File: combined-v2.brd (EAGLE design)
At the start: 0 parts

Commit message: v2 of board finished
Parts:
- added 100POT1_COMP1, 100POT1_COMP2, 100POT1_COMP3, 100POT1_COMP5: MCP42100-I/P, MCP42100-I_P:DIP254P762X432-14
- added 10KPOT1_PAN1, 10KPOT1_PAN2, 10KPOT1_PAN3, 10KPOT1_PAN4, 10POT1_COMP1, 10POT1_COMP2, 10POT1_COMP3, 10POT1_COMP5, 10POT2_COMP1, 10POT2_COMP2, 10POT2_COMP3, 10POT2_COMP5: MCP4131-503E/SN, MCP4131-503E_SN:SOIC127P599X175-8N
- added 200POT1_COMP1, 200POT1_COMP2, 200POT1_COMP3, 200POT1_COMP5, 200POT2_COMP1, 200POT2_COMP2, 200POT2_COMP3, 200POT2_COMP5: MAX5419LETA+, MAX5419LETA_:SON65P300X300X80-9N
- added 3V3_D1, 9VDD1, BCK_ADC1, CE_EQ1, CE_EQ2, CLK_ADC1, CS3, CS4, CS5, CS6, DOUT_ADC1, GND4, GND6, LRCK_ADC1, MUX2, MUX3, PAD1, PAD10, PAD11, PAD12, PAD13, PAD14, PAD15, PAD16, PAD2, PAD3, PAD4, PAD5, PAD6, PAD7, PAD8, PAD9, SCK1, SCL1, SCL2, SDA1, SDA2, SDI/O1: (no value), wirepad:SMD1,27-2,54
- added C10, C105, C106, C109, C11, C110, C111, C112, C115, C116, C14, C15, C16, C17, C20, C21: 0.01uF, rcl:C0402
- added C103, C104, C117, C118, C22, C23, C7, C9: 0.047uF, rcl:C0402
- added C107, C108, C113, C114, C12, C13, C18, C19: 0.068uF, rcl:C0402
- added C119, C120, C121, C122, C123, C124, C125, C126, C127, C129, C130, C131, C132, C134, C2, C24, C25, C26, C27, C28, C29, C30, C31, C32, C34, C35, C36, C37, C39, C5, C6, C69, C71, C77, C78, C79, C8, C80, C81, C82, C83, C84: 10uF, rcl:C0402
- added C128, C133, C33, C38, C68, C70, C73: 0.1uF, rcl:C0402
- added C3, C4: 0.1u, rcl:C0402
- added C42, C45, C48, C54: 680p, rcl:C0402
- added C43, C46, C49, C55: 10u, rcl:C0402
- added C44, C47, C50, C56: 1.5u, rcl:C0402
- added C72, C74: 1uF, rcl:C0402
- added C75, C76: 15pF, rcl:C0402
- added D16, D17, D18, D19, D20, D21, D22, D23, D24, D25, D26, D27, D28, D29, D30, D31, D32, D33, D34, D35, D36, D37, D38, D39, D40, D41, D42, D43, D44, D45, D46, D47, D48, D60, D61, D62, D63, D64, D65, D66, D67, D68, D69, D70: 1N4148W-TP, 1N4148W-TP:SOD123
- added D2, D3, D4, D5: 1N4148W-TPSOD123-L, 1N4148W-TP:SOD123-L
- added GND1, GND2, GND3, GND5, GNDL1, GNDR1, IN_COMP1, IN_COMP2, IN_COMP3, IN_COMP5, OUTL_MIX1, OUTR_MIX1: (no value), wirepad:SMD2,54-5,08
- added IC2: PCM1865DBT, PCM1865DBT:TSSOP-30
- added OPAMP1_COMP1, OPAMP1_COMP2, OPAMP1_COMP3, OPAMP1_COMP5, OPAMP1_MIX1, OPAMP1_PAN1, OPAMP1_PAN2, OPAMP1_PAN3, OPAMP1_PAN4, OPAMP2_COMP1, OPAMP2_COMP2, OPAMP2_COMP3, OPAMP2_COMP5, OPAMP3_COMP1, OPAMP3_COMP2, OPAMP3_COMP3, OPAMP3_COMP5, OPAMP4_COMP1, OPAMP4_COMP2, OPAMP4_COMP3, OPAMP4_COMP5, U2: LM4562MAX/NOPB, LM4562MAX_NOPB:SOIC127P599X175-8N
- added R10, R11, R13, R16, R17, R18, R20, R31, R33, R35, R36, R37, R38, R39, R40, R43, R46, R48, R50, R51, R52, R53, R54, R55, R58, R69, R7, R70, R71, R73, R83, R84, R85, R87: 5k, rcl:R0402
- added R100, R102, R103, R104, R107, R108, R109, R111, R112, R113, R117, R118, R120, R121, R122, R125, R126, R127, R129, R130, R149, R153, R154, R156, R157, R158, R161, R162, R163, R165, R166, R63, R67, R75, R77, R78, R79, R89, R90, R91, R93, R94, R95, R99: 100k, rcl:R0402
- added R101, R105, R110, R119, R12, R123, R128, R14, R155, R159, R164, R19, R21, R32, R34, R41, R42, R47, R49, R56, R57, R72, R74, R76, R80, R86, R88, R92: 10k, rcl:R0402
- added R106, R124, R160, R81: 20k, rcl:R0402
- added R114, R116, R150, R152, R64, R66, R96, R98: 470k, rcl:R0402
- added R115, R151, R45, R5, R60, R65, R8, R9, R97: 1k, rcl:R0402
- added R15, R6, R68, R82: 1M, rcl:R0402
- added R22: 1.7k, rcl:R0402
- added R44, R59: 50k, rcl:R0402
- added U$1, U$3: LC75281E, LC75281E:QFP80P1720X1720X270-64N
- added U11, U3, U4, U5: TMUX1204DGSR, TMUX1204DGSR:SOP50P490X110-10N
- added Y2: CM7V-T1A-32.768KHZ-12.5PF-100PPM-TB-QC, CM7V-T1A-32.768KHZ-12.5PF-100PPM-TB-QC:XTAL_CM7V-T1A-32.768KHZ-12.5PF-100PPM-TB-QC
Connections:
- new net +3V3: 3V3_D1.1, U11.5, U11.6, U3.5, U3.6, U4.5, U4.6, U5.5, U5.6
- new net 3V3A: C70.1, C71.1, IC2.8, U2.1, U2.2
- new net 3V3D: C68.1, C69.1, IC2.13, IC2.14
- new net BCK_ADC: BCK_ADC1.1, IC2.17
- new net CLK_ADC: CLK_ADC1.1, IC2.15
- new net CS: CS6.1, U11.8
- new net CS0: CS3.1, U3.8
- new net CS0_COMP1: 100POT1_COMP1.1, U3.2
- new net CS0_COMP2: 100POT1_COMP3.1, U3.9
- new net CS0_COMP3: 100POT1_COMP2.1, U3.4
- new net CS0_COMP4: 100POT1_COMP5.1, U3.7
- new net CS1: CS4.1, U5.8
- new net CS1_COMP1: 10POT1_COMP1.1, U5.2
- new net CS1_COMP2: 10POT1_COMP3.1, U5.9
- new net CS1_COMP3: 10POT1_COMP2.1, U5.4
- new net CS1_COMP4: 10POT1_COMP5.1, U5.7
- new net CS2: CS5.1, U4.8
- new net CS2_COMP1: 10POT2_COMP1.1, U4.2
- new net CS2_COMP2: 10POT2_COMP3.1, U4.9
- new net CS2_COMP3: 10POT2_COMP2.1, U4.4
- new net CS2_COMP4: 10POT2_COMP5.1, U4.7
- new net CS_PAN1: 10KPOT1_PAN1.1, U11.2
- new net CS_PAN2: 10KPOT1_PAN3.1, U11.9
- new net CS_PAN3: 10KPOT1_PAN2.1, U11.4
- new net CS_PAN4: 10KPOT1_PAN4.1, U11.7
- new net DOUT_ADC: DOUT_ADC1.1, IC2.18
- new net EQ1_CE1: CE_EQ1.1, U$1.27
- new net EQ2_CE3: CE_EQ2.1, U$3.27
- new net GND: 100POT1_COMP1.4, 100POT1_COMP2.4, 100POT1_COMP3.4, 100POT1_COMP5.4, 10KPOT1_PAN1.4, 10KPOT1_PAN2.4, 10KPOT1_PAN3.4, 10KPOT1_PAN4.4, 10POT1_COMP1.4, 10POT1_COMP2.4, 10POT1_COMP3.4, 10POT1_COMP5.4, 10POT2_COMP1.4, 10POT2_COMP2.4, 10POT2_COMP3.4, 10POT2_COMP5.4, 200POT1_COMP1.5, 200POT1_COMP1.9, 200POT1_COMP2.5, 200POT1_COMP2.9, 200POT1_COMP3.5, 200POT1_COMP3.9, 200POT1_COMP5.5, 200POT1_COMP5.9, 200POT2_COMP1.4, 200POT2_COMP1.5, 200POT2_COMP1.9, 200POT2_COMP2.4, 200POT2_COMP2.5, 200POT2_COMP2.9, 200POT2_COMP3.4, 200POT2_COMP3.5, 200POT2_COMP3.9, 200POT2_COMP5.4, 200POT2_COMP5.5, 200POT2_COMP5.9, C123.2, C134.2, C28.2, C39.2, C68.2, C69.2, C70.2, C71.2, C72.2, C73.2, C74.2, C75.2, C76.2, GND1.1, GND2.1, GND3.1, GND4.1, GND5.1, GND6.1, GNDL1.1, GNDR1.1, IC2.12, IC2.25, IC2.7, OPAMP1_COMP1.4, OPAMP1_COMP2.4, OPAMP1_COMP3.4, OPAMP1_COMP5.4, OPAMP1_MIX1.4, OPAMP1_PAN1.4, OPAMP1_PAN2.4, OPAMP1_PAN3.4, OPAMP1_PAN4.4, OPAMP2_COMP1.4, OPAMP2_COMP2.4, OPAMP2_COMP3.4, OPAMP2_COMP5.4, OPAMP3_COMP1.4, OPAMP3_COMP2.4, OPAMP3_COMP3.4, OPAMP3_COMP5.4, OPAMP4_COMP1.4, OPAMP4_COMP2.4, OPAMP4_COMP3.4, OPAMP4_COMP5.4, R5.1, R9.1, U$1.21, U$1.28, U$3.21, U$3.28, U11.3, U2.4, U3.3, U4.3, U5.3
- new net H1_COMP1: 200POT1_COMP1.8, 200POT2_COMP1.8, C44.1, OPAMP1_COMP1.6, R66.1
- new net H1_COMP2: 200POT1_COMP3.8, 200POT2_COMP3.8, C50.1, OPAMP1_COMP3.6, R116.1
- new net H1_COMP3: 200POT1_COMP2.8, 200POT2_COMP2.8, C47.1, OPAMP1_COMP2.6, R98.1
- new net H1_COMP4: 200POT1_COMP5.8, 200POT2_COMP5.8, C56.1, OPAMP1_COMP5.6, R152.1
- new net IN_COMP1: C43.2, IN_COMP1.1
- new net IN_COMP2: C49.2, IN_COMP3.1
- new net IN_COMP3: C46.2, IN_COMP2.1
- new net IN_COMP4: C55.2, IN_COMP5.1
- new net L1_COMP1: 200POT1_COMP1.6, 200POT1_COMP1.7, D19.C
- new net L1_COMP2: 200POT1_COMP3.6, 200POT1_COMP3.7, D41.C
- new net L1_COMP3: 200POT1_COMP2.6, 200POT1_COMP2.7, D30.C
- new net L1_COMP4: 200POT1_COMP5.6, 200POT1_COMP5.7, D63.C
- new net L2_COMP1: 200POT2_COMP1.6, 200POT2_COMP1.7, R94.2
- new net L2_COMP2: 200POT2_COMP3.6, 200POT2_COMP3.7, R130.2
- new net L2_COMP3: 200POT2_COMP2.6, 200POT2_COMP2.7, R112.2
- new net L2_COMP4: 200POT2_COMP5.6, 200POT2_COMP5.7, R166.2
- new net LRCK_ADC: IC2.16, LRCK_ADC1.1
- new net MUX0: MUX2.1, U11.1, U3.1, U4.1, U5.1
- new net MUX1: MUX3.1, U11.10, U3.10, U4.10, U5.10
- new net N$10: R32.2, R34.2, R41.2, R42.2, R43.1
- new net N$100: D64.A, D65.C
- new net N$101: C55.1, R163.2
- new net N$102: D68.A, D69.C
- new net N$103: D67.A, D68.C
- new net N$11: R31.2, R38.1, R42.1
- new net N$114: C72.1, IC2.6
- new net N$115: C73.1, C74.1, IC2.11
- new net N$116: C75.1, IC2.9, Y2.2
- new net N$117: C76.1, IC2.10, Y2.1
- new net N$118: C84.2, IC2.1
- new net N$119: C77.2, IC2.2
- new net N$12: R33.2, R37.1, R41.1
- new net N$120: C103.1, U$3.1
- new net N$121: C105.1, U$3.6
- new net N$122: C106.1, U$3.7
- new net N$123: C81.2, IC2.3
- new net N$124: C107.1, U$3.11
- new net N$125: C78.2, IC2.4
- new net N$126: C79.2, IC2.29
- new net N$127: C83.2, IC2.28
- new net N$128: C80.2, IC2.27
- new net N$13: C13.1, U$1.12
- new net N$131: C108.1, U$3.12
- new net N$132: C109.1, U$3.16
- new net N$135: C110.1, U$3.17
- new net N$136: C111.1, U$3.32
- new net N$137: C112.1, U$3.33
- new net N$138: C113.1, U$3.37
- new net N$139: C114.1, U$3.38
- new net N$14: C14.1, U$1.16
- new net N$140: C115.1, U$3.42
- new net N$141: C116.1, U$3.43
- new net N$142: C117.1, U$3.47
- new net N$143: C118.1, U$3.48
- new net N$144: C103.2, U$3.64
- new net N$145: C104.2, C119.2, U$3.3
- new net N$146: C119.1, U$3.4
- new net N$147: C120.1, U$3.9
- new net N$148: C121.1, U$3.14
- new net N$149: C122.1, U$3.19
- new net N$15: C15.1, U$1.17
- new net N$150: C123.1, C134.1, U$3.23
- new net N$151: C124.1, U$3.30
- new net N$152: C125.1, U$3.35
- new net N$153: C126.1, U$3.40
- new net N$154: C127.1, U$3.45
- new net N$155: C128.1, U$3.50
- new net N$156: C129.1, U$3.52
- new net N$157: C130.1, U$3.55
- new net N$158: C131.1, U$3.59
- new net N$159: C132.1, U$3.62
- new net N$16: C16.1, U$1.32
- new net N$160: C133.1, U$3.63
- new net N$161: C105.2, U$3.5
- new net N$162: C106.2, C120.2, U$3.8
- new net N$163: C107.2, U$3.10
- new net N$164: C108.2, C121.2, U$3.13
- new net N$165: C109.2, U$3.15
- new net N$166: C110.2, C122.2, U$3.18
- new net N$167: C111.2, C124.2, U$3.31
- new net N$168: C112.2, U$3.34
- new net N$169: C113.2, C125.2, U$3.36
- new net N$17: C17.1, U$1.33
- new net N$170: C114.2, U$3.39
- new net N$171: C115.2, C126.2, U$3.41
- new net N$172: C116.2, U$3.44
- new net N$173: C117.2, C127.2, U$3.46
- new net N$174: C118.2, U$3.49
- new net N$175: C129.2, U$3.51
- new net N$176: C130.2, U$3.54
- new net N$177: C131.2, U$3.58
- new net N$178: C132.2, U$3.61
- new net N$179: C104.1, U$3.2
- new net N$18: R34.1, R36.1, R40.2
- new net N$183: C82.2, IC2.30
- new net N$19: C4.1, R60.2
- new net N$2: C2.2, R10.2, R6.2, R7.2
- new net N$20: R47.1, R50.2, R54.2
- new net N$21: R47.2, R49.2, R56.2, R57.2, R58.1
- new net N$211: C42.1, D17.A, D18.C, D25.A, R65.1, R89.2
- new net N$212: C48.1, D39.A, D40.C, D47.A, R115.1, R125.2
- new net N$213: C45.1, D28.A, D29.C, D36.A, R107.2, R97.1
- new net N$214: C54.1, D61.A, D62.C, D69.A, R151.1, R161.2
- new net N$22: R46.2, R53.1, R57.1
- new net N$23: R48.2, R52.1, R56.1
- new net N$24: R49.1, R51.1, R55.2
- new net N$25: C18.1, U$1.37
- new net N$26: C6.2, R68.2, R69.2, R70.2
- new net N$27: C19.1, U$1.38
- new net N$28: C8.2, R82.2, R83.2, R84.2
- new net N$29: C20.1, U$1.42
- new net N$3: C5.2, R15.2, R16.2, R17.2
- new net N$30: C21.1, U$1.43
- new net N$31: C22.1, U$1.47
- new net N$32: C23.1, U$1.48
- new net N$33: C7.2, U$1.64
- new net N$34: C24.2, C9.2, U$1.3
- new net N$35: C24.1, U$1.4
- new net N$36: C25.1, U$1.9
- new net N$37: C26.1, U$1.14
- new net N$38: C27.1, U$1.19
- new net N$39: C28.1, C39.1, U$1.23
- new net N$4: C7.1, U$1.1
- new net N$40: C29.1, U$1.30
- new net N$41: C30.1, U$1.35
- new net N$42: C31.1, U$1.40
- new net N$43: C32.1, U$1.45
- new net N$44: C33.1, U$1.50
- new net N$45: C34.1, U$1.52
- new net N$46: C35.1, U$1.55
- new net N$47: C36.1, U$1.59
- new net N$48: C37.1, U$1.62
- new net N$49: C38.1, U$1.63
- new net N$5: C10.1, U$1.6
- new net N$50: C10.2, U$1.5
- new net N$51: C11.2, C25.2, U$1.8
- new net N$52: C12.2, U$1.10
- new net N$53: C13.2, C26.2, U$1.13
- new net N$54: C14.2, U$1.15
- new net N$55: C15.2, C27.2, U$1.18
- new net N$56: C16.2, C29.2, U$1.31
- new net N$57: C17.2, U$1.34
- new net N$58: C18.2, C30.2, U$1.36
- new net N$59: C19.2, U$1.39
- new net N$6: C11.1, U$1.7
- new net N$60: C20.2, C31.2, U$1.41
- new net N$61: C21.2, U$1.44
- new net N$62: C22.2, C32.2, U$1.46
- new net N$63: C23.2, U$1.49
- new net N$64: C34.2, U$1.51
- new net N$65: C35.2, U$1.54
- new net N$66: C36.2, U$1.58
- new net N$67: C37.2, U$1.61
- new net N$68: C9.1, U$1.2
- new net N$7: C12.1, U$1.11
- new net N$70: R22.2, R9.2, U2.3
- new net N$71: R5.2, R8.2, U2.5
- new net N$74: D16.A, D17.C
- new net N$75: D21.A, D22.C
- new net N$76: D20.A, D21.C
- new net N$77: C43.1, R91.2
- new net N$78: D24.A, D25.C
- new net N$79: D23.A, D24.C
- new net N$8: C3.1, R45.2
- new net N$80: D27.A, D28.C
- new net N$81: D32.A, D33.C
- new net N$82: D31.A, D32.C
- new net N$83: C46.1, R109.2
- new net N$84: D35.A, D36.C
- new net N$85: D34.A, D35.C
- new net N$86: D38.A, D39.C
- new net N$87: D43.A, D44.C
- new net N$88: D42.A, D43.C
- new net N$89: C49.1, R127.2
- new net N$9: R32.1, R35.2, R39.2
- new net N$90: D46.A, D47.C
- new net N$91: D45.A, D46.C
- new net N$98: D60.A, D61.C
- new net N$99: D65.A, D66.C
- new net NEG_A1_COMP1: C42.2, D16.C, D18.A, OPAMP1_COMP1.2, R63.2
- new net NEG_A1_COMP2: C48.2, D38.C, D40.A, OPAMP1_COMP3.2, R113.2
- new net NEG_A1_COMP3: C45.2, D27.C, D29.A, OPAMP1_COMP2.2, R95.2
- new net NEG_A1_COMP4: C54.2, D60.C, D62.A, OPAMP1_COMP5.2, R149.2
- new net NEG_A2_COMP1: OPAMP2_COMP1.2, R67.2, R75.1
- new net NEG_A2_COMP2: OPAMP2_COMP3.2, R117.2, R118.1
- new net NEG_A2_COMP3: OPAMP2_COMP2.2, R100.1, R99.2
- new net NEG_A2_COMP4: OPAMP2_COMP5.2, R153.2, R154.1
- new net NEG_A3_COMP1: OPAMP3_COMP1.2, R77.1, R78.2
- new net NEG_A3_COMP2: OPAMP3_COMP3.2, R120.1, R121.2
- new net NEG_A3_COMP3: OPAMP3_COMP2.2, R102.1, R103.2
- new net NEG_A3_COMP4: OPAMP3_COMP5.2, R156.1, R157.2
- new net NEG_A4_COMP1: OPAMP4_COMP1.2, R79.2, R80.2
- new net NEG_A4_COMP2: OPAMP4_COMP3.2, R122.2, R123.2
- new net NEG_A4_COMP3: OPAMP4_COMP2.2, R104.2, R105.2
- new net NEG_A4_COMP4: OPAMP4_COMP5.2, R158.2, R159.2
- new net NEG_A_MIX: OPAMP1_MIX1.2, R43.2, R44.1
- new net NEG_A_PAN1: OPAMP1_PAN1.2, R71.1, R74.1
- new net NEG_A_PAN2: OPAMP1_PAN3.2, R85.1, R88.1
- new net NEG_A_PAN3: OPAMP1_PAN2.2, R11.1, R14.1
- new net NEG_A_PAN4: OPAMP1_PAN4.2, R18.1, R21.1
- new net NEG_B2_COMP1: OPAMP2_COMP1.6, OPAMP2_COMP1.7, R93.2
- new net NEG_B2_COMP2: OPAMP2_COMP3.6, OPAMP2_COMP3.7, R129.2
- new net NEG_B2_COMP3: OPAMP2_COMP2.6, OPAMP2_COMP2.7, R111.2
- new net NEG_B2_COMP4: OPAMP2_COMP5.6, OPAMP2_COMP5.7, R165.2
- new net NEG_B3_COMP1: OPAMP3_COMP1.6, R89.1, R90.2
- new net NEG_B3_COMP2: OPAMP3_COMP3.6, R125.1, R126.2
- new net NEG_B3_COMP3: OPAMP3_COMP2.6, R107.1, R108.2
- new net NEG_B3_COMP4: OPAMP3_COMP5.6, R161.1, R162.2
- new net NEG_B4_COMP1: 100POT1_COMP1.5, OPAMP4_COMP1.6, R81.2
- new net NEG_B4_COMP2: 100POT1_COMP3.5, OPAMP4_COMP3.6, R124.2
- new net NEG_B4_COMP3: 100POT1_COMP2.5, OPAMP4_COMP2.6, R106.2
- new net NEG_B4_COMP4: 100POT1_COMP5.5, OPAMP4_COMP5.6, R160.2
- new net NEG_B_MIX: OPAMP1_MIX1.6, R58.2, R59.1
- new net NEG_B_PAN1: OPAMP1_PAN1.6, R72.2, R73.2
- new net NEG_B_PAN2: OPAMP1_PAN3.6, R86.2, R87.2
- new net NEG_B_PAN3: OPAMP1_PAN2.6, R12.2, R13.2
- new net NEG_B_PAN4: OPAMP1_PAN4.6, R19.2, R20.2
- new net OUT1_EQ1: C33.2, C6.1, PAD16.1
- new net OUT1_EQ2: C128.2, C5.1, PAD14.1
- new net OUT2_EQ1: C38.2, C8.1, PAD15.1
- new net OUT2_EQ2: C133.2, C2.1, PAD13.1
- new net OUTL_MIX1: C3.2, OUTL_MIX1.1
- new net OUTL_PAN1: C79.1, OPAMP1_PAN1.1, PAD3.1, R55.1, R74.2
- new net OUTL_PAN2: C80.1, OPAMP1_PAN3.1, PAD5.1, R31.1, R88.2
- new net OUTL_PAN3: C78.1, OPAMP1_PAN2.1, PAD1.1, R14.2, R46.1
- new net OUTL_PAN4: C84.1, OPAMP1_PAN4.1, PAD7.1, R21.2, R40.1
- new net OUTR_MIX1: C4.2, OUTR_MIX1.1
- new net OUTR_PAN1: C82.1, OPAMP1_PAN1.7, PAD6.1, R33.1, R72.1
- new net OUTR_PAN2: C83.1, OPAMP1_PAN3.7, PAD4.1, R54.1, R86.1
- new net OUTR_PAN3: C81.1, OPAMP1_PAN2.7, PAD8.1, R12.1, R39.1
- new net OUTR_PAN4: C77.1, OPAMP1_PAN4.7, PAD2.1, R19.1, R48.1
- new net OUT_A1_COMP1: OPAMP1_COMP1.1, R65.2
- new net OUT_A1_COMP2: OPAMP1_COMP3.1, R115.2
- new net OUT_A1_COMP3: OPAMP1_COMP2.1, R97.2
- new net OUT_A1_COMP4: OPAMP1_COMP5.1, R151.2
- new net OUT_A2_COMP1: 100POT1_COMP1.10, OPAMP2_COMP1.1, R75.2
- new net OUT_A2_COMP2: 100POT1_COMP3.10, OPAMP2_COMP3.1, R118.2
- new net OUT_A2_COMP3: 100POT1_COMP2.10, OPAMP2_COMP2.1, R100.2
- new net OUT_A2_COMP4: 100POT1_COMP5.10, OPAMP2_COMP5.1, R154.2
- new net OUT_A3_COMP1: D26.A, OPAMP3_COMP1.1
- new net OUT_A3_COMP2: D48.A, OPAMP3_COMP3.1
- new net OUT_A3_COMP3: D37.A, OPAMP3_COMP2.1
- new net OUT_A3_COMP4: D70.A, OPAMP3_COMP5.1
- new net OUT_A4_COMP1: OPAMP4_COMP1.1, OPAMP4_COMP1.5, R78.1, R79.1
- new net OUT_A4_COMP2: OPAMP4_COMP3.1, OPAMP4_COMP3.5, R121.1, R122.1
- new net OUT_A4_COMP3: OPAMP4_COMP2.1, OPAMP4_COMP2.5, R103.1, R104.1
- new net OUT_A4_COMP4: OPAMP4_COMP5.1, OPAMP4_COMP5.5, R157.1, R158.1
- new net OUT_A_MIX: OPAMP1_MIX1.1, R44.2, R45.1
- new net OUT_B1_COMP1: D19.A, OPAMP1_COMP1.7
- new net OUT_B1_COMP2: D41.A, OPAMP1_COMP3.7
- new net OUT_B1_COMP3: D30.A, OPAMP1_COMP2.7
- new net OUT_B1_COMP4: D63.A, OPAMP1_COMP5.7
- new net OUT_B3_COMP1: D20.C, OPAMP3_COMP1.7, R90.1
- new net OUT_B3_COMP2: D42.C, OPAMP3_COMP3.7, R126.1
- new net OUT_B3_COMP3: D31.C, OPAMP3_COMP2.7, R108.1
- new net OUT_B3_COMP4: D64.C, OPAMP3_COMP5.7, R162.1
- new net OUT_B_MIX: OPAMP1_MIX1.7, R59.2, R60.1
- new net OUT_COMP1: 100POT1_COMP1.6, 100POT1_COMP1.7, OPAMP4_COMP1.7, PAD10.1, U$1.60
- new net OUT_COMP2: 100POT1_COMP3.6, 100POT1_COMP3.7, OPAMP4_COMP3.7, PAD9.1, U$1.53
- new net OUT_COMP3: 100POT1_COMP2.6, 100POT1_COMP2.7, OPAMP4_COMP2.7, PAD12.1, U$3.60
- new net OUT_COMP4: 100POT1_COMP5.6, 100POT1_COMP5.7, OPAMP4_COMP5.7, PAD11.1, U$3.53
- new net P0A1_COMP1: 10POT1_COMP1.5, R76.2
- new net P0A1_COMP2: 10POT1_COMP3.5, R119.2
- new net P0A1_COMP3: 10POT1_COMP2.5, R101.2
- new net P0A1_COMP4: 10POT1_COMP5.5, R155.2
- new net P0A2_COMP1: 10POT2_COMP1.5, R92.1
- new net P0A2_COMP2: 10POT2_COMP3.5, R128.1
- new net P0A2_COMP3: 10POT2_COMP2.5, R110.1
- new net P0A2_COMP4: 10POT2_COMP5.5, R164.1
- new net P0A_PAN1: 10KPOT1_PAN1.5, R70.1, R71.2
- new net P0A_PAN2: 10KPOT1_PAN3.5, R84.1, R85.2
- new net P0A_PAN3: 10KPOT1_PAN2.5, R10.1, R11.2
- new net P0A_PAN4: 10KPOT1_PAN4.5, R17.1, R18.2
- new net P0B_PAN1: 10KPOT1_PAN1.7, R69.1, R73.1
- new net P0B_PAN2: 10KPOT1_PAN3.7, R83.1, R87.1
- new net P0B_PAN3: 10KPOT1_PAN2.7, R13.1, R7.1
- new net P0B_PAN4: 10KPOT1_PAN4.7, R16.1, R20.1
- new net P0W1_COMP1: 10POT1_COMP1.6, R67.1
- new net P0W1_COMP2: 10POT1_COMP3.6, R117.1
- new net P0W1_COMP3: 10POT1_COMP2.6, R99.1
- new net P0W1_COMP4: 10POT1_COMP5.6, R153.1
- new net P0W_PAN1: 10KPOT1_PAN1.6, D2.1
- new net P0W_PAN2: 10KPOT1_PAN3.6, D4.1
- new net P0W_PAN3: 10KPOT1_PAN2.6, D3.1
- new net P0W_PAN4: 10KPOT1_PAN4.6, D5.1
- new net POS_A1_COMP1: 100POT1_COMP1.9, OPAMP1_COMP1.3
- new net POS_A1_COMP2: 100POT1_COMP3.9, OPAMP1_COMP3.3
- new net POS_A1_COMP3: 100POT1_COMP2.9, OPAMP1_COMP2.3
- new net POS_A1_COMP4: 100POT1_COMP5.9, OPAMP1_COMP5.3
- new net POS_A2_COMP1: OPAMP2_COMP1.3, R64.2, R66.2
- new net POS_A2_COMP2: OPAMP2_COMP3.3, R114.2, R116.2
- new net POS_A2_COMP3: OPAMP2_COMP2.3, R96.2, R98.2
- new net POS_A2_COMP4: OPAMP2_COMP5.3, R150.2, R152.2
- new net POS_A4_COMP1: D22.A, D23.C, OPAMP4_COMP1.3, R93.1
- new net POS_A4_COMP2: D44.A, D45.C, OPAMP4_COMP3.3, R129.1
- new net POS_A4_COMP3: D33.A, D34.C, OPAMP4_COMP2.3, R111.1
- new net POS_A4_COMP4: D66.A, D67.C, OPAMP4_COMP5.3, R165.1
- new net POS_B1_COMP1: D26.C, OPAMP1_COMP1.5, R77.2
- new net POS_B1_COMP2: D48.C, OPAMP1_COMP3.5, R120.2
- new net POS_B1_COMP3: D37.C, OPAMP1_COMP2.5, R102.2
- new net POS_B1_COMP4: D70.C, OPAMP1_COMP5.5, R156.2
- new net POS_B2_COMP1: 10POT2_COMP1.6, 10POT2_COMP1.7, OPAMP2_COMP1.5, R91.1
- new net POS_B2_COMP2: 10POT2_COMP3.6, 10POT2_COMP3.7, OPAMP2_COMP3.5, R127.1
- new net POS_B2_COMP3: 10POT2_COMP2.6, 10POT2_COMP2.7, OPAMP2_COMP2.5, R109.1
- new net POS_B2_COMP4: 10POT2_COMP5.6, 10POT2_COMP5.7, OPAMP2_COMP5.5, R163.1
- new net SCK: 100POT1_COMP1.2, 100POT1_COMP2.2, 100POT1_COMP3.2, 100POT1_COMP5.2, 10KPOT1_PAN1.2, 10KPOT1_PAN2.2, 10KPOT1_PAN3.2, 10KPOT1_PAN4.2, 10POT1_COMP1.2, 10POT1_COMP2.2, 10POT1_COMP3.2, 10POT1_COMP5.2, 10POT2_COMP1.2, 10POT2_COMP2.2, 10POT2_COMP3.2, 10POT2_COMP5.2, SCK1.1, U$1.25, U$3.25
- new net SCL: 200POT1_COMP1.2, 200POT1_COMP2.2, 200POT1_COMP3.2, 200POT1_COMP5.2, 200POT2_COMP1.2, 200POT2_COMP2.2, 200POT2_COMP3.2, 200POT2_COMP5.2, SCL1.1
- new net SCL1: IC2.24, SCL2.1
- new net SDA: 200POT1_COMP1.3, 200POT1_COMP2.3, 200POT1_COMP3.3, 200POT1_COMP5.3, 200POT2_COMP1.3, 200POT2_COMP2.3, 200POT2_COMP3.3, 200POT2_COMP5.3, SDA1.1
- new net SDA1: IC2.23, SDA2.1
- new net SDI/O: 100POT1_COMP1.3, 100POT1_COMP2.3, 100POT1_COMP3.3, 100POT1_COMP5.3, 10KPOT1_PAN1.3, 10KPOT1_PAN2.3, 10KPOT1_PAN3.3, 10KPOT1_PAN4.3, 10POT1_COMP1.3, 10POT1_COMP2.3, 10POT1_COMP3.3, 10POT1_COMP5.3, 10POT2_COMP1.3, 10POT2_COMP2.3, 10POT2_COMP3.3, 10POT2_COMP5.3, SDI/O1.1, U$1.26, U$3.26
- new net VDD: 9VDD1.1, OPAMP1_COMP1.8, OPAMP1_COMP2.8, OPAMP1_COMP3.8, OPAMP1_COMP5.8, OPAMP1_MIX1.8, OPAMP1_PAN1.8, OPAMP1_PAN2.8, OPAMP1_PAN3.8, OPAMP1_PAN4.8, OPAMP2_COMP1.8, OPAMP2_COMP2.8, OPAMP2_COMP3.8, OPAMP2_COMP5.8, OPAMP3_COMP1.8, OPAMP3_COMP2.8, OPAMP3_COMP3.8, OPAMP3_COMP5.8, OPAMP4_COMP1.8, OPAMP4_COMP2.8, OPAMP4_COMP3.8, OPAMP4_COMP5.8, R101.1, R119.1, R155.1, R22.1, R76.1, R8.1, U$1.22, U$3.22, U2.8
- new net VREF: 100POT1_COMP1.11, 100POT1_COMP1.12, 100POT1_COMP1.14, 100POT1_COMP1.8, 100POT1_COMP2.11, 100POT1_COMP2.12, 100POT1_COMP2.14, 100POT1_COMP2.8, 100POT1_COMP3.11, 100POT1_COMP3.12, 100POT1_COMP3.14, 100POT1_COMP3.8, 100POT1_COMP5.11, 100POT1_COMP5.12, 100POT1_COMP5.14, 100POT1_COMP5.8, 10KPOT1_PAN1.8, 10KPOT1_PAN2.8, 10KPOT1_PAN3.8, 10KPOT1_PAN4.8, 10POT1_COMP1.7, 10POT1_COMP1.8, 10POT1_COMP2.7, 10POT1_COMP2.8, 10POT1_COMP3.7, 10POT1_COMP3.8, 10POT1_COMP5.7, 10POT1_COMP5.8, 10POT2_COMP1.8, 10POT2_COMP2.8, 10POT2_COMP3.8, 10POT2_COMP5.8, 200POT1_COMP1.1, 200POT1_COMP1.4, 200POT1_COMP2.1, 200POT1_COMP2.4, 200POT1_COMP3.1, 200POT1_COMP3.4, 200POT1_COMP5.1, 200POT1_COMP5.4, 200POT2_COMP1.1, 200POT2_COMP2.1, 200POT2_COMP3.1, 200POT2_COMP5.1, C44.2, C47.2, C50.2, C56.2, D2.2, D3.2, D4.2, D5.2, OPAMP1_MIX1.3, OPAMP1_MIX1.5, OPAMP1_PAN1.3, OPAMP1_PAN1.5, OPAMP1_PAN2.3, OPAMP1_PAN2.5, OPAMP1_PAN3.3, OPAMP1_PAN3.5, OPAMP1_PAN4.3, OPAMP1_PAN4.5, OPAMP3_COMP1.3, OPAMP3_COMP1.5, OPAMP3_COMP2.3, OPAMP3_COMP2.5, OPAMP3_COMP3.3, OPAMP3_COMP3.5, OPAMP3_COMP5.3, OPAMP3_COMP5.5, R105.1, R106.1, R110.2, R112.1, R113.1, R114.1, R123.1, R124.1, R128.2, R130.1, R149.1, R15.1, R150.1, R159.1, R160.1, R164.2, R166.1, R35.1, R36.2, R37.2, R38.2, R50.1, R51.2, R52.2, R53.2, R6.1, R63.1, R64.1, R68.1, R80.1, R81.1, R82.1, R92.2, R94.1, R95.1, R96.1, U2.6, U2.7
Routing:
- net VREF: track 0.00 -> 1081.0 mm, vias 0 -> 62
- net VDD: track 0.00 -> 704.9 mm, vias 0 -> 24
- net SDI/O: track 0.00 -> 623.2 mm, vias 0 -> 14
- net SCK: track 0.00 -> 589.0 mm, vias 0 -> 14
- net OUTR_PAN1: track 0.00 -> 394.1 mm, vias 0 -> 1
- net OUTR_PAN4: track 0.00 -> 369.8 mm, vias 0 -> 1
- net GND: track 0.00 -> 299.6 mm, vias 0 -> 43
- net OUTL_PAN2: track 0.00 -> 180.7 mm, vias 0 -> 1
- net CS0_COMP3: track 0.00 -> 169.9 mm, vias 0 -> 2
- net OUTR_PAN2: track 0.00 -> 165.9 mm, vias 0 -> 1
- net CS_PAN1: track 0.00 -> 153.6 mm, vias 0 -> 4
- net OUTL_PAN4: track 0.00 -> 147.9 mm, vias 0 -> 1
- net CS_PAN2: track 0.00 -> 144.2 mm, vias 0 -> 2
- net OUTL_PAN1: track 0.00 -> 131.3 mm, vias 0 -> 1
- net OUTL_PAN3: track 0.00 -> 126.3 mm, vias 0 -> 1
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- added copper zone on layer 2, net GND
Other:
- board outline added: 128.3 x 142.2 mm

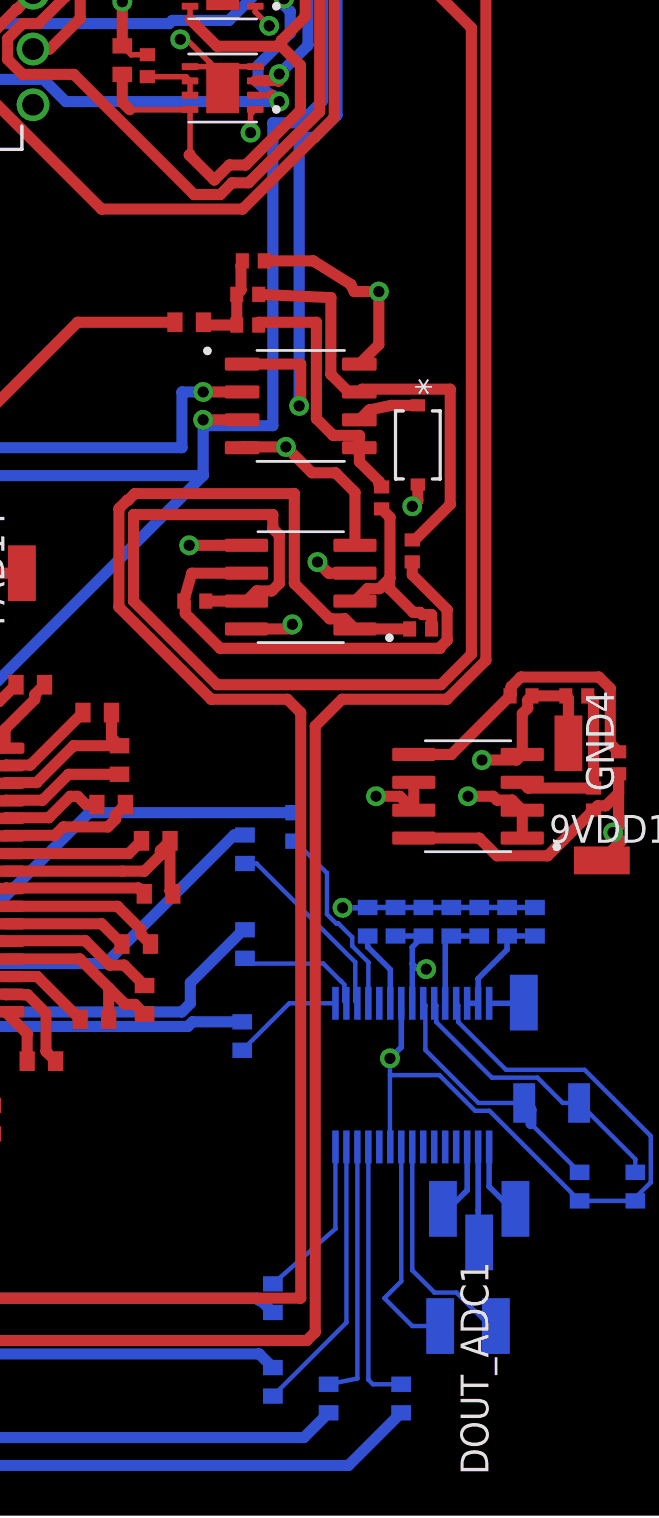
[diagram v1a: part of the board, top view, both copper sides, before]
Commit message: update footprint names of MAX5419 for LMNP variants
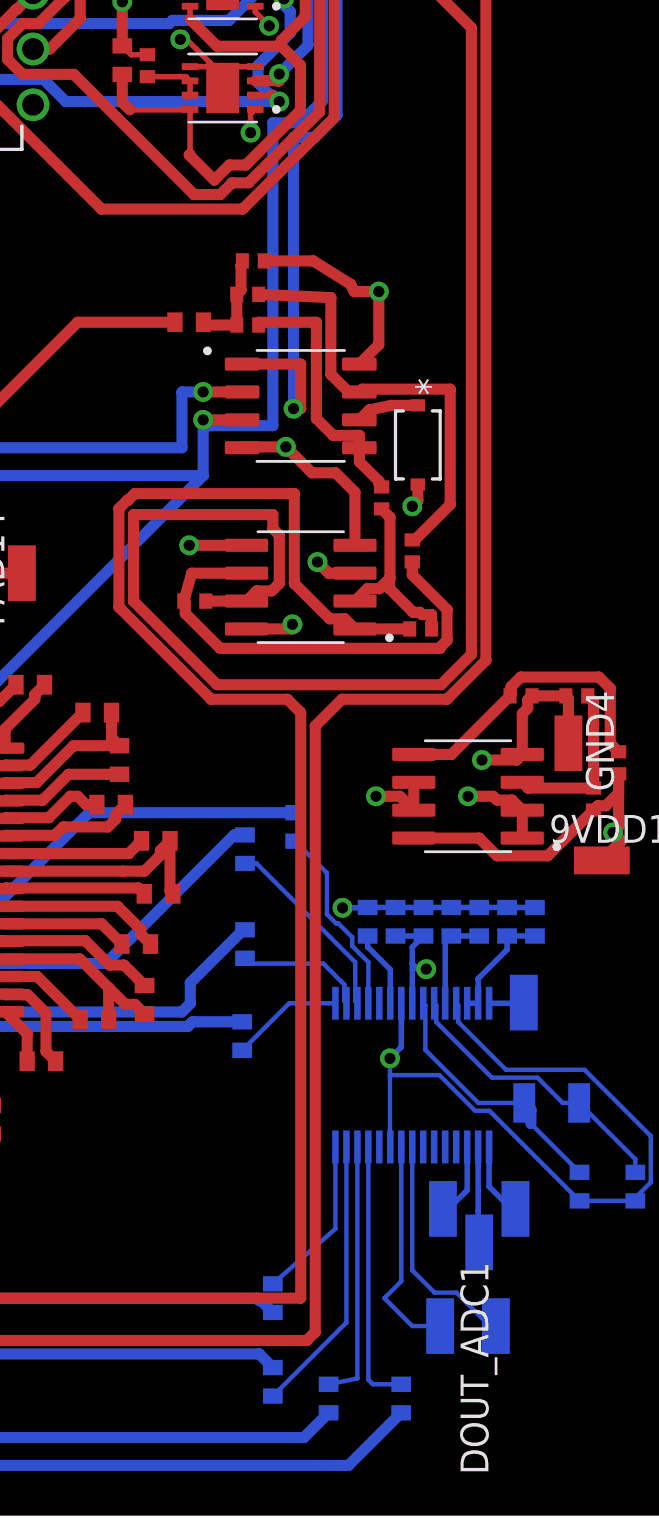
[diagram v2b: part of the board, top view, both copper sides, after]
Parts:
- 200POT1_COMP1, 200POT2_COMP1: value MAX5419LETA+ -> MAX5419NETA+; device MAX5419LETA_:SON65P300X300X80-9N -> MAX5419NETA_:SON65P300X300X80-9N
- 200POT1_COMP2, 200POT2_COMP2: value MAX5419LETA+ -> MAX5419META+
- 200POT1_COMP3, 200POT2_COMP3: value MAX5419LETA+ -> MAX5419PETAT; device MAX5419LETA_:SON65P300X300X80-9N -> MAX5419PETAT:SON65P300X300X80-9N
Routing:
- net CS_PAN4: track 125.4 -> 126.2 mm

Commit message: update CAM
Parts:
- Y2: value CM7V-T1A-32.768KHZ-12.5PF-100PPM-TB-QC -> ECS-245.7-20-3X-EN-TR; device CM7V-T1A-32.768KHZ-12.5PF-100PPM-TB-QC:XTAL_CM7V-T1A-32.768KHZ-12.5PF-100PPM-TB-QC -> ECS-245.7-20-3X-EN-TR:XTAL_ECS-245.7-20-3X-EN-TR
- moved Y2 3.59 mm to (106.7, 68.6), turned to 270 degrees
- moved C76 1.27 mm to (106.7, 62.2)
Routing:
- net N$117: track 13.1 -> 21.7 mm
- net GND: track 299.6 -> 295.7 mm
- net N$116: track 11.9 -> 15.1 mm

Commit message: fixes and export using jlcpcb ulp
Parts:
- C3, C4: value 0.1u -> 0.1uF
- C43, C46, C49, C55: value 10u -> 10uF
- D2, D3, D4, D5: value 1N4148W-TPSOD123-L -> 1N4148W-TP; device 1N4148W-TP:SOD123-L -> 1N4148W-TP:SOD123
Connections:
- net P0W_PAN1: now also D2.C; no longer D2.1
- net P0W_PAN2: now also D4.C; no longer D4.1
- net P0W_PAN3: now also D3.C; no longer D3.1
- net P0W_PAN4: now also D5.C; no longer D5.1
- net VREF: now also D2.A, D3.A, D4.A, D5.A; no longer D2.2, D3.2, D4.2, D5.2
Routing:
- net VREF: track 1081.0 -> 1082.2 mm
- net P0B_PAN4: track 20.3 -> 21.2 mm
- net P0B_PAN3: track 19.6 -> 20.1 mm
- net P0B_PAN2: track 19.6 -> 20.1 mm
- net P0B_PAN1: track 19.6 -> 20.1 mm

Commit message: fix on cap units
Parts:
- C42, C45, C48, C54: value 680p -> 680pF
- C44, C47, C50, C56: value 1.5u -> 1.5uF
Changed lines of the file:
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@@
 <drawing>
 <settings>
-<setting alwaysvectorfont="no"/>
+<setting alwaysvectorfont="yes"/>
 <setting verticaltext="up"/>
 </settings>
@@
 <attribute name="VALUE" x="69.469" y="61.341" size="1.27" layer="27" rot="R180"/>
 </element>
-<element name="C42" library="rcl" library_urn="urn:adsk.eagle:library:334" package="C0402" package3d_urn="urn:adsk.eagle:package:23626/2" value="680p" x="2.667" y="131.064" smashed="yes">
+<element name="C42" library="rcl" library_urn="urn:adsk.eagle:library:334" package="C0402" package3d_urn="urn:adsk.eagle:package:23626/2" value="680pF" x="2.667" y="131.064" smashed="yes">
 <attribute name="NAME" x="2.032" y="131.699" size="1.27" layer="25" display="off"/>
 <attribute name="POPULARITY" value="16" x="69.977" y="66.294" size="1.778" layer="27" display="off"/>
@@
 <attribute name="VALUE" x="-2.921" y="160.274" size="1.27" layer="27" rot="R90"/>
 </element>
-<element name="C44" library="rcl" library_urn="urn:adsk.eagle:library:334" package="C0402" package3d_urn="urn:adsk.eagle:package:23626/2" value="1.5u" x="5.842" y="109.728" smashed="yes" rot="R90">
+<element name="C44" library="rcl" library_urn="urn:adsk.eagle:library:334" package="C0402" package3d_urn="urn:adsk.eagle:package:23626/2" value="1.5uF" x="5.842" y="109.728" smashed="yes" rot="R90">
 <attribute name="NAME" x="5.207" y="109.093" size="1.27" layer="25" rot="R90" display="off"/>
 <attribute name="POPULARITY" value="16" x="82.042" y="141.478" size="1.778" layer="27" rot="R90" display="off"/>
@@
 <attribute name="VALUE" x="5.08" y="110.109" size="1.27" layer="27" rot="R270"/>
 </element>
-<element name="C48" library="rcl" library_urn="urn:adsk.eagle:library:334" package="C0402" package3d_urn="urn:adsk.eagle:package:23626/2" value="680p" x="26.797" y="132.334" smashed="yes">
+<element name="C48" library="rcl" library_urn="urn:adsk.eagle:library:334" package="C0402" package3d_urn="urn:adsk.eagle:package:23626/2" value="680pF" x="26.797" y="132.334" smashed="yes">
 <attribute name="NAME" x="26.162" y="132.969" size="1.27" layer="25" display="off"/>
 <attribute name="POPULARITY" value="16" x="94.107" y="67.564" size="1.778" layer="27" display="off"/>
@@
 <attribute name="VALUE" x="21.209" y="161.544" size="1.27" layer="27" rot="R90"/>
 </element>
-<element name="C50" library="rcl" library_urn="urn:adsk.eagle:library:334" package="C0402" package3d_urn="urn:adsk.eagle:package:23626/2" value="1.5u" x="29.972" y="110.998" smashed="yes" rot="R90">
+<element name="C50" library="rcl" library_urn="urn:adsk.eagle:library:334" package="C0402" package3d_urn="urn:adsk.eagle:package:23626/2" value="1.5uF" x="29.972" y="110.998" smashed="yes" rot="R90">
 <attribute name="NAME" x="29.337" y="110.363" size="1.27" layer="25" rot="R90" display="off"/>
 <attribute name="POPULARITY" value="16" x="106.172" y="142.748" size="1.778" layer="27" rot="R90" display="off"/>
@@
 <attribute name="VALUE" x="29.21" y="111.379" size="1.27" layer="27" rot="R270"/>
 </element>
-<element name="C45" library="rcl" library_urn="urn:adsk.eagle:library:334" package="C0402" package3d_urn="urn:adsk.eagle:package:23626/2" value="680p" x="53.467" y="132.334" smashed="yes">
+<element name="C45" library="rcl" library_urn="urn:adsk.eagle:library:334" package="C0402" package3d_urn="urn:adsk.eagle:package:23626/2" value="680pF" x="53.467" y="132.334" smashed="yes">
 <attribute name="NAME" x="52.832" y="132.969" size="1.27" layer="25" display="off"/>
 <attribute name="POPULARITY" value="16" x="120.777" y="67.564" size="1.778" layer="27" display="off"/>
@@
 <attribute name="VALUE" x="47.879" y="161.544" size="1.27" layer="27" rot="R90"/>
 </element>
-<element name="C47" library="rcl" library_urn="urn:adsk.eagle:library:334" package="C0402" package3d_urn="urn:adsk.eagle:package:23626/2" value="1.5u" x="56.642" y="110.998" smashed="yes" rot="R90">
+<element name="C47" library="rcl" library_urn="urn:adsk.eagle:library:334" package="C0402" package3d_urn="urn:adsk.eagle:package:23626/2" value="1.5uF" x="56.642" y="110.998" smashed="yes" rot="R90">
 <attribute name="NAME" x="56.007" y="110.363" size="1.27" layer="25" rot="R90" display="off"/>
 <attribute name="POPULARITY" value="16" x="132.842" y="142.748" size="1.778" layer="27" rot="R90" display="off"/>
@@
 <attribute name="VALUE" x="55.88" y="111.379" size="1.27" layer="27" rot="R270"/>
 </element>
-<element name="C54" library="rcl" library_urn="urn:adsk.eagle:library:334" package="C0402" package3d_urn="urn:adsk.eagle:package:23626/2" value="680p" x="81.407" y="134.874" smashed="yes">
+<element name="C54" library="rcl" library_urn="urn:adsk.eagle:library:334" package="C0402" package3d_urn="urn:adsk.eagle:package:23626/2" value="680pF" x="81.407" y="134.874" smashed="yes">
 <attribute name="NAME" x="80.772" y="135.509" size="1.27" layer="25" display="off"/>
 <attribute name="POPULARITY" value="16" x="148.717" y="70.104" size="1.778" layer="27" display="off"/>
@@
 <attribute name="VALUE" x="75.819" y="164.084" size="1.27" layer="27" rot="R90"/>
 </element>
-<element name="C56" library="rcl" library_urn="urn:adsk.eagle:library:334" package="C0402" package3d_urn="urn:adsk.eagle:package:23626/2" value="1.5u" x="84.582" y="113.538" smashed="yes" rot="R90">
+<element name="C56" library="rcl" library_urn="urn:adsk.eagle:library:334" package="C0402" package3d_urn="urn:adsk.eagle:package:23626/2" value="1.5uF" x="84.582" y="113.538" smashed="yes" rot="R90">
 <attribute name="NAME" x="83.947" y="112.903" size="1.27" layer="25" rot="R90" display="off"/>
 <attribute name="POPULARITY" value="16" x="160.782" y="145.288" size="1.778" layer="27" rot="R90" display="off"/>

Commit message: update power resisitors
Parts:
- R22: value 1.7k -> 17k
- R5, R8, R9: value 1k -> 10k
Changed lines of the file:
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@@
 <drawing>
 <settings>
-<setting alwaysvectorfont="yes"/>
+<setting alwaysvectorfont="no"/>
 <setting verticaltext="up"/>
 </settings>
@@
 <attribute name="VALUE" x="83.82" y="113.919" size="1.27" layer="27" rot="R270"/>
 </element>
-<element name="R5" library="rcl" library_urn="urn:adsk.eagle:library:334" package="R0402" package3d_urn="urn:adsk.eagle:package:23547/3" value="1k" x="102.743" y="84.582" smashed="yes" rot="R180">
+<element name="R5" library="rcl" library_urn="urn:adsk.eagle:library:334" package="R0402" package3d_urn="urn:adsk.eagle:package:23547/3" value="10k" x="102.743" y="84.582" smashed="yes" rot="R180">
 <attribute name="NAME" x="103.378" y="83.947" size="1.27" layer="25" rot="R180" display="off"/>
 <attribute name="POPULARITY" value="34" x="82.423" y="97.282" size="1.778" layer="27" rot="R180" display="off"/>
@@
 <attribute name="VALUE" x="103.378" y="86.487" size="1.27" layer="27" rot="R180"/>
 </element>
-<element name="R8" library="rcl" library_urn="urn:adsk.eagle:library:334" package="R0402" package3d_urn="urn:adsk.eagle:package:23547/3" value="1k" x="107.188" y="81.534" smashed="yes" rot="R90">
+<element name="R8" library="rcl" library_urn="urn:adsk.eagle:library:334" package="R0402" package3d_urn="urn:adsk.eagle:package:23547/3" value="10k" x="107.188" y="81.534" smashed="yes" rot="R90">
 <attribute name="NAME" x="106.553" y="80.899" size="1.27" layer="25" rot="R90" display="off"/>
 <attribute name="POPULARITY" value="34" x="119.888" y="105.664" size="1.778" layer="27" rot="R90" display="off"/>
@@
 <attribute name="VALUE" x="109.093" y="80.899" size="1.27" layer="27" rot="R90"/>
 </element>
-<element name="R9" library="rcl" library_urn="urn:adsk.eagle:library:334" package="R0402" package3d_urn="urn:adsk.eagle:package:23547/3" value="1k" x="105.283" y="84.582" smashed="yes">
+<element name="R9" library="rcl" library_urn="urn:adsk.eagle:library:334" package="R0402" package3d_urn="urn:adsk.eagle:package:23547/3" value="10k" x="105.283" y="84.582" smashed="yes">
 <attribute name="NAME" x="104.648" y="85.217" size="1.27" layer="25" display="off"/>
 <attribute name="POPULARITY" value="34" x="120.523" y="66.802" size="1.778" layer="27" display="off"/>
@@
 <attribute name="VALUE" x="104.648" y="82.677" size="1.27" layer="27"/>
 </element>
-<element name="R22" library="rcl" library_urn="urn:adsk.eagle:library:334" package="R0402" package3d_urn="urn:adsk.eagle:package:23547/3" value="1.7k" x="106.045" y="79.883" smashed="yes" rot="R90">
+<element name="R22" library="rcl" library_urn="urn:adsk.eagle:library:334" package="R0402" package3d_urn="urn:adsk.eagle:package:23547/3" value="17k" x="106.045" y="79.883" smashed="yes" rot="R90">
 <attribute name="NAME" x="105.41" y="79.248" size="1.27" layer="25" rot="R90" display="off"/>
 <attribute name="POPULARITY" value="34" x="118.745" y="96.393" size="1.778" layer="27" rot="R90" display="off"/>
